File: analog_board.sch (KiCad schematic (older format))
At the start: 54 parts, among them J301 SAMTEC-TSW-105-07-X-D, J302 SAMTEC-TSW-105-07-X-D, J304 SAMTEC-TSW-105-07-X-D, J305 SAMTEC-TSW-105-07-X-D, U1 LM324, U3 AD620, U4 AD620

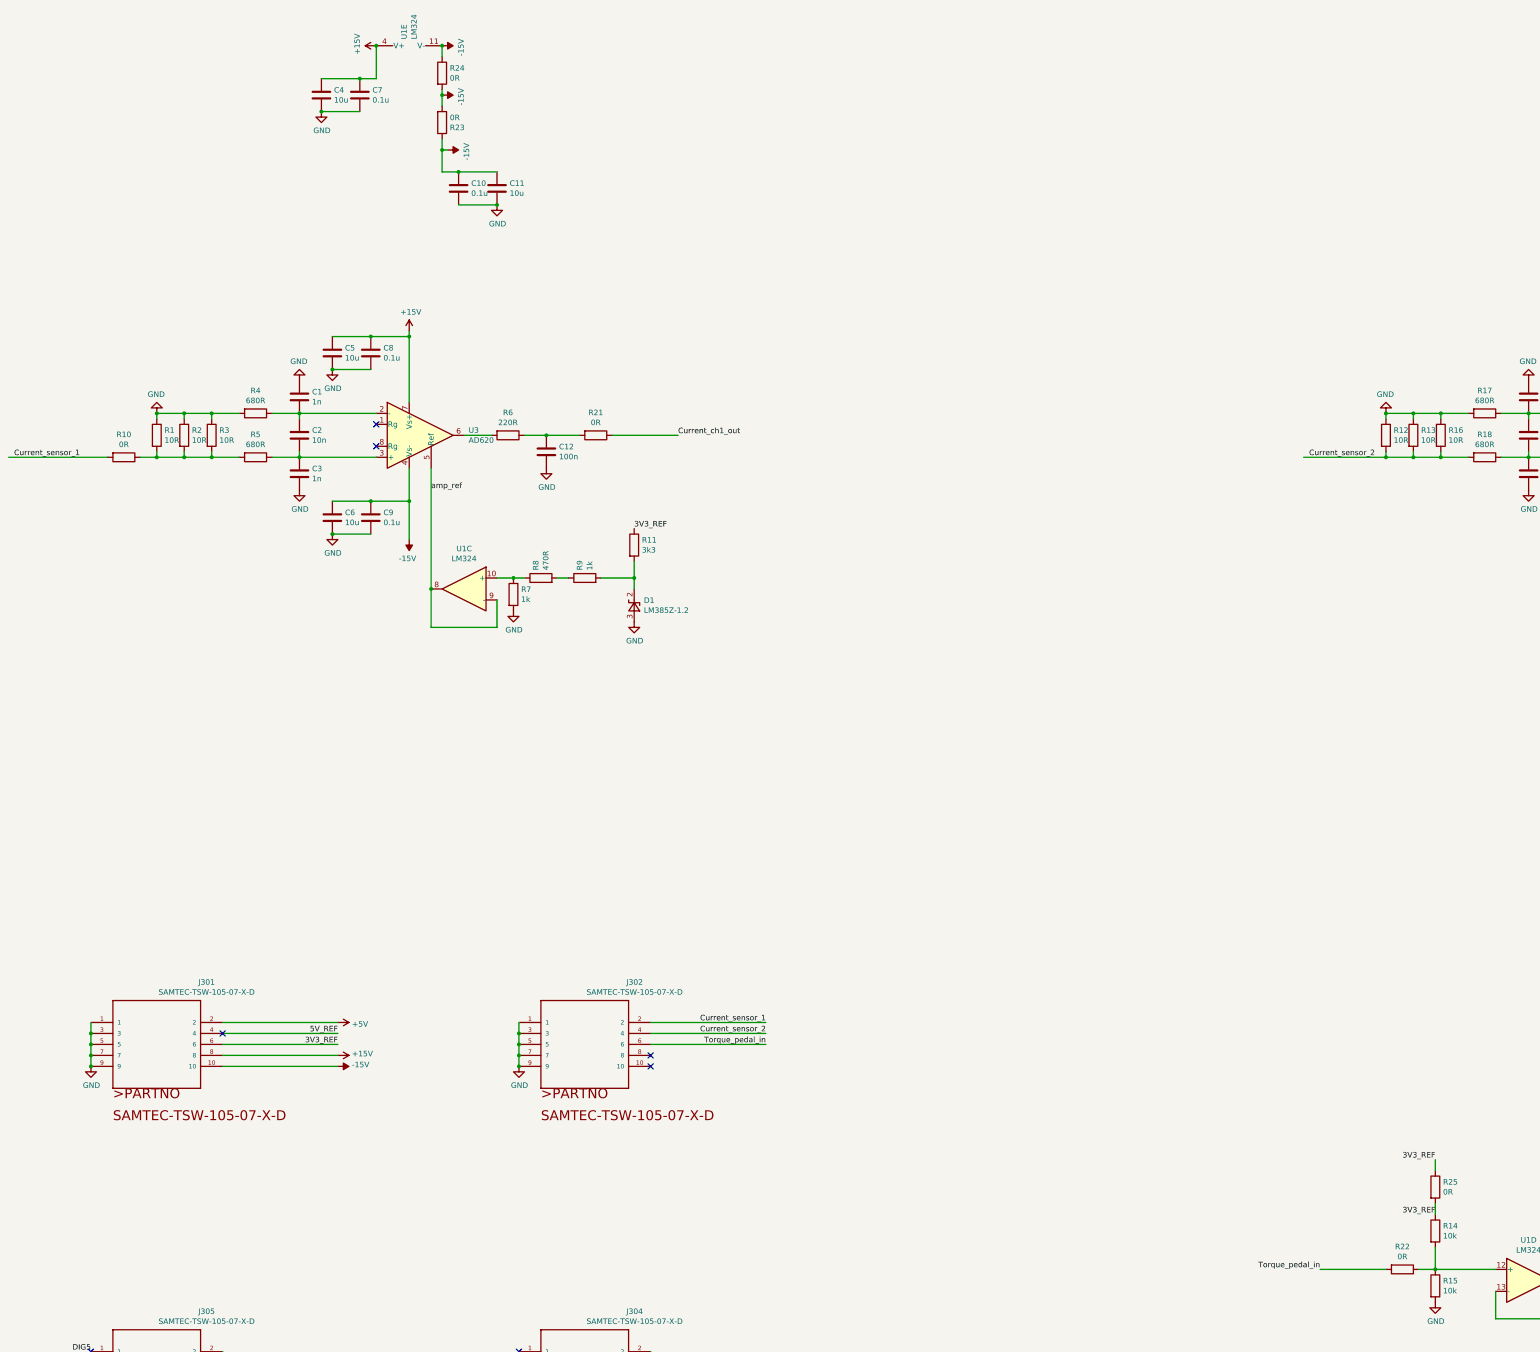
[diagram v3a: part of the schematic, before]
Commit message: Removed OR jumers. Realigned connectors. Moved large components to Bottom. Thickened tracks.
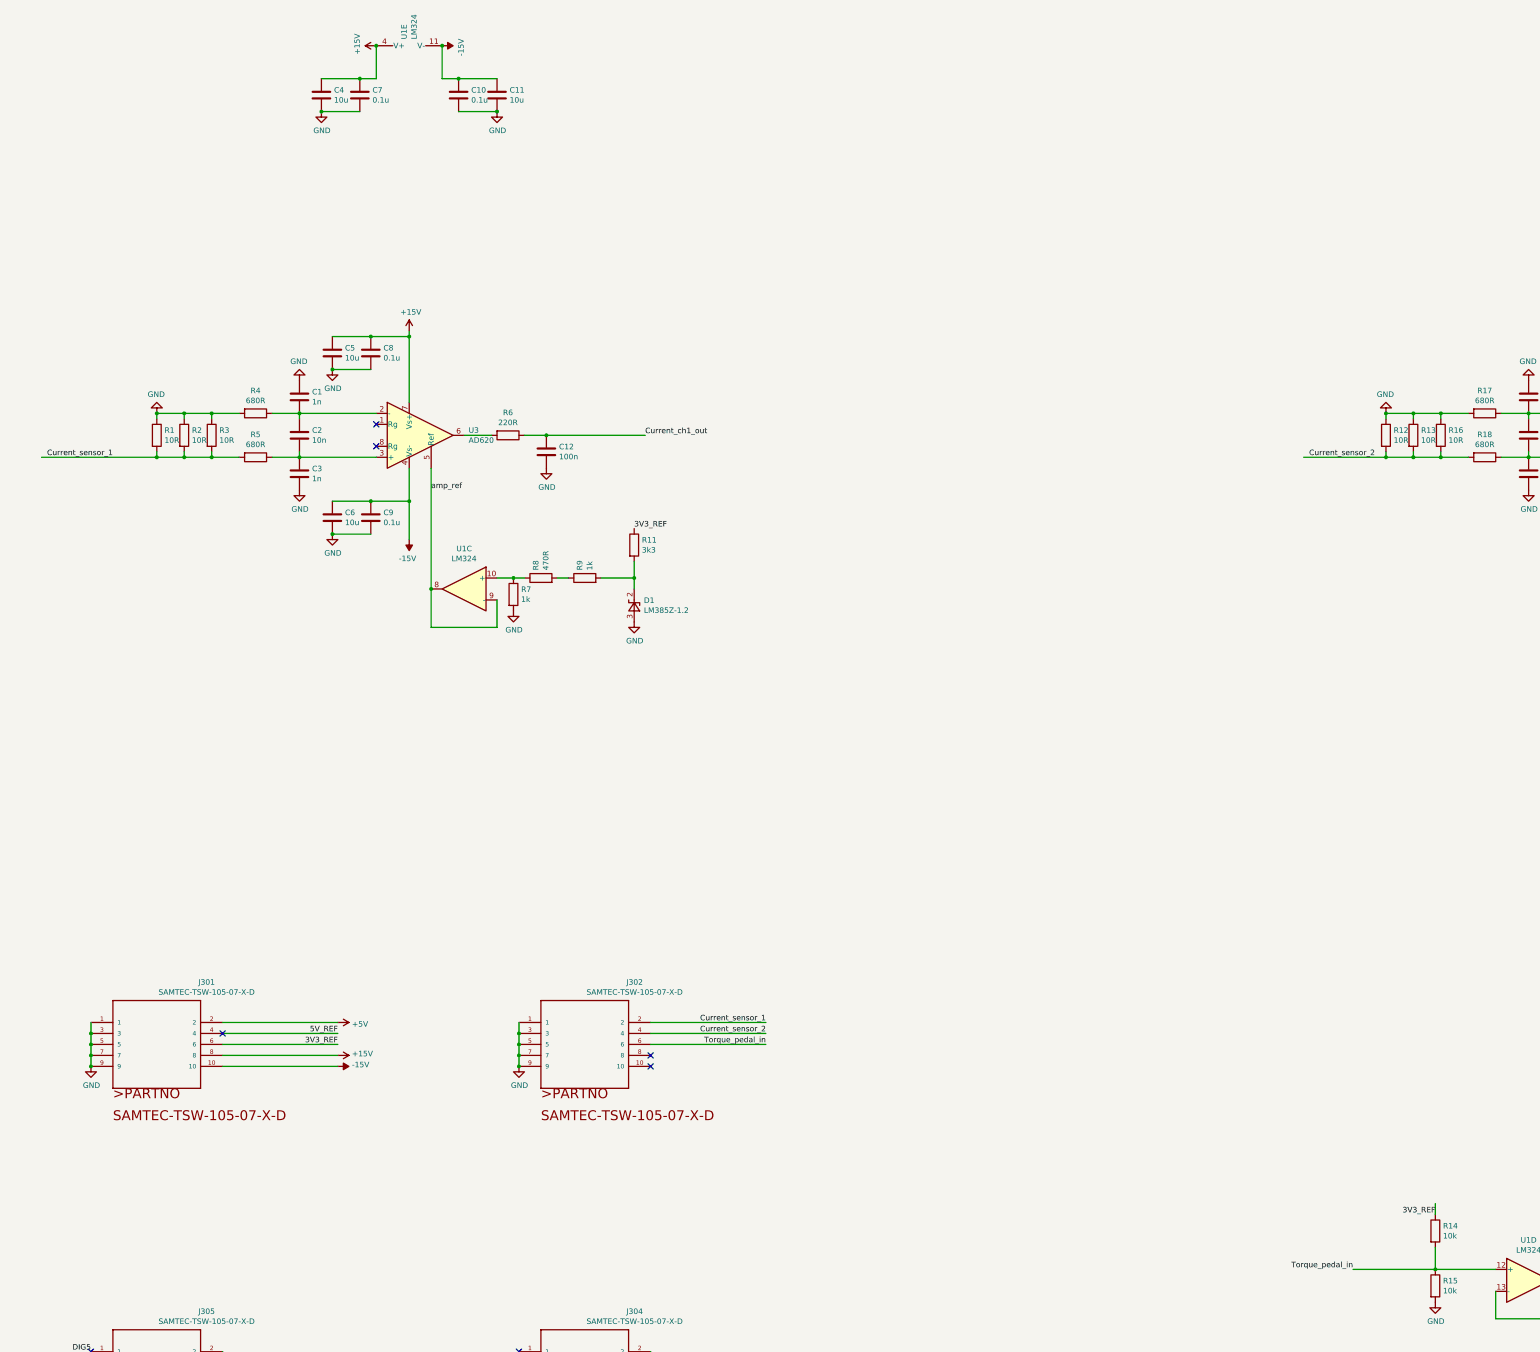
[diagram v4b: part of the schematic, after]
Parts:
- removed R10, R21, R22, R24, R25: 0R, Resistor_SMD:R_1206_3216Metric_Pad1.42x1.75mm_HandSolder, symbol Device:R
- removed R23: 0R, Resistor_SMD:R_0805_2012Metric_Pad1.15x1.40mm_HandSolder, symbol Device:R
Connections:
- net Current_ch1_out: now also C12.1, R6.1
- net Current_sensor_1: now also R1.2, R2.2, R3.2, R5.2
- net Torque_pedal_in: now also R14.2, R15.1, U1.12 (+)
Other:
- moved on the sheet: C10, C11
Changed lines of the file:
@@
 	1    0    0    -1
 $EndComp
-Text Label 850  4800 0    50   ~ 0
+Text Label 1150 4800 0    50   ~ 0
 Current_sensor_1
 $Comp
@@
 Wire Wire Line
 	5250 6100 5250 6350
-Wire Wire Line
-	6900 4600 6300 4600
-Text Label 6900 4600 0    50   ~ 0
+Text Label 6600 4600 0    50   ~ 0
 Current_ch1_out
 Wire Wire Line
@@
 L Device:C C11
 U 1 1 5C74975A
-P 5250 2350
-F 0 "C11" H 5365 2396 50  0000 L CNN
-F 1 "10u" H 5365 2305 50  0000 L CNN
-F 2 "Capacitor_SMD:C_0805_2012Metric_Pad1.15x1.40mm_HandSolder" H 5288 2200 50  0001 C CNN
-F 3 "~" H 5250 2350 50  0001 C CNN
-	1    5250 2350
+P 5250 1500
+F 0 "C11" H 5365 1546 50  0000 L CNN
+F 1 "10u" H 5365 1455 50  0000 L CNN
+F 2 "Capacitor_SMD:C_0805_2012Metric_Pad1.15x1.40mm_HandSolder" H 5288 1350 50  0001 C CNN
+F 3 "~" H 5250 1500 50  0001 C CNN
+	1    5250 1500
 	1    0    0    -1
 $EndComp
@@
 L power:GND #PWR0116
 U 1 1 5C749765
-P 5250 2500
-F 0 "#PWR0116" H 5250 2250 50  0001 C CNN
-F 1 "GND" H 5255 2327 50  0000 C CNN
-F 2 "" H 5250 2500 50  0001 C CNN
-F 3 "" H 5250 2500 50  0001 C CNN
-	1    5250 2500
+P 5250 1650
+F 0 "#PWR0116" H 5250 1400 50  0001 C CNN
+F 1 "GND" H 5255 1477 50  0000 C CNN
+F 2 "" H 5250 1650 50  0001 C CNN
+F 3 "" H 5250 1650 50  0001 C CNN
+	1    5250 1650
 	1    0    0    -1
 $EndComp
@@
 L Device:C C10
 U 1 1 5C7542C0
-P 4900 2350
-F 0 "C10" H 5015 2396 50  0000 L CNN
-F 1 "0.1u" H 5015 2305 50  0000 L CNN
-F 2 "Capacitor_SMD:C_0805_2012Metric_Pad1.15x1.40mm_HandSolder" H 4938 2200 50  0001 C CNN
-F 3 "~" H 4900 2350 50  0001 C CNN
-	1    4900 2350
-	1    0    0    -1
-$EndComp
-Wire Wire Line
-	4900 2200 5250 2200
-Wire Wire Line
-	4900 2500 5250 2500
-Connection ~ 5250 2500
+P 4900 1500
+F 0 "C10" H 5015 1546 50  0000 L CNN
+F 1 "0.1u" H 5015 1455 50  0000 L CNN
+F 2 "Capacitor_SMD:C_0805_2012Metric_Pad1.15x1.40mm_HandSolder" H 4938 1350 50  0001 C CNN
+F 3 "~" H 4900 1500 50  0001 C CNN
+	1    4900 1500
+	1    0    0    -1
+$EndComp
+Wire Wire Line
+	4900 1350 5250 1350
+Wire Wire Line
+	4900 1650 5250 1650
+Connection ~ 5250 1650
 Wire Wire Line
 	4000 1350 4150 1350
@@
 Connection ~ 4150 1050
 Wire Wire Line
-	4900 2200 4750 2200
-Wire Wire Line
-	4750 2200 4750 2000
-Connection ~ 4900 2200
+	4900 1350 4750 1350
+Connection ~ 4900 1350
 $Comp
 L power:+5V #PWR0117
@@
 	1    0    0    -1
 $EndComp
-Text Label 13800 11200 2    50   ~ 0
-3V3_REF
-Text Label 12750 12200 2    50   ~ 0
+Text Label 13050 12200 2    50   ~ 0
 Torque_pedal_in
 Wire Wire Line
@@
 Wire Wire Line
 	15850 4900 15850 5100
-$Comp
-L Device:R R10
-U 1 1 5C792D0B
-P 1850 4800
-F 0 "R10" V 1643 4800 50  0000 C CNN
-F 1 "0R" V 1734 4800 50  0000 C CNN
-F 2 "Resistor_SMD:R_1206_3216Metric_Pad1.42x1.75mm_HandSolder" V 1780 4800 50  0001 C CNN
-F 3 "~" H 1850 4800 50  0001 C CNN
-	1    1850 4800
-	0    1    1    0
-$EndComp
-Wire Wire Line
-	800  4800 1700 4800
-Wire Wire Line
-	2000 4800 2150 4800
 Connection ~ 2150 4800
-$Comp
-L Device:R R21
-U 1 1 5C7A1976
-P 6150 4600
-F 0 "R21" V 5943 4600 50  0000 C CNN
-F 1 "0R" V 6034 4600 50  0000 C CNN
-F 2 "Resistor_SMD:R_1206_3216Metric_Pad1.42x1.75mm_HandSolder" V 6080 4600 50  0001 C CNN
-F 3 "~" H 6150 4600 50  0001 C CNN
-	1    6150 4600
-	0    1    1    0
-$EndComp
-Wire Wire Line
-	5700 4600 6000 4600
 Connection ~ 5700 4600
-$Comp
-L Device:R R22
-U 1 1 5C7B8DFC
-P 13500 12200
-F 0 "R22" V 13293 12200 50  0000 C CNN
-F 1 "0R" V 13384 12200 50  0000 C CNN
-F 2 "Resistor_SMD:R_1206_3216Metric_Pad1.42x1.75mm_HandSolder" V 13430 12200 50  0001 C CNN
-F 3 "~" H 13500 12200 50  0001 C CNN
-	1    13500 12200
-	0    1    1    0
-$EndComp
-Wire Wire Line
-	13800 12200 13650 12200
-Wire Wire Line
-	13350 12200 12750 12200
-$Comp
-L Device:R R23
-U 1 1 5C7D3DFD
-P 4750 1750
-F 0 "R23" H 4820 1796 50  0000 L CNN
-F 1 "0R" H 4820 1705 50  0000 L CNN
-F 2 "Resistor_SMD:R_0805_2012Metric_Pad1.15x1.40mm_HandSolder" V 4680 1750 50  0001 C CNN
-F 3 "~" H 4750 1750 50  0001 C CNN
-	1    4750 1750
-	1    0    0    1
-$EndComp
-$Comp
-L power:-15V #PWR0128
-U 1 1 5C7F0418
-P 4800 2000
-F 0 "#PWR0128" H 4800 2100 50  0001 C CNN
-F 1 "-15V" H 4815 2173 50  0000 C CNN
-F 2 "" H 4800 2000 50  0001 C CNN
-F 3 "" H 4800 2000 50  0001 C CNN
-	1    4800 2000
-	0    1    1    0
-$EndComp
-Wire Wire Line
-	4800 2000 4750 2000
-Connection ~ 4750 2000
-Wire Wire Line
-	4750 2000 4750 1900
-$Comp
-L Device:R R24
-U 1 1 5C80067D
-P 4750 1300
-F 0 "R24" H 4820 1346 50  0000 L CNN
-F 1 "0R" H 4820 1255 50  0000 L CNN
-F 2 "Resistor_SMD:R_1206_3216Metric_Pad1.42x1.75mm_HandSolder" V 4680 1300 50  0001 C CNN
-F 3 "~" H 4750 1300 50  0001 C CNN
-	1    4750 1300
-	1    0    0    -1
-$EndComp
-Wire Wire Line
-	4750 1150 4750 1050
 Connection ~ 4750 1050
 Wire Wire Line
-	4750 1450 4750 1500
-$Comp
-L Device:R R25
-U 1 1 5C7CD4AE
-P 13800 11450
-F 0 "R25" H 13870 11496 50  0000 L CNN
-F 1 "0R" H 13870 11405 50  0000 L CNN
-F 2 "Resistor_SMD:R_1206_3216Metric_Pad1.42x1.75mm_HandSolder" V 13730 11450 50  0001 C CNN
-F 3 "~" H 13800 11450 50  0001 C CNN
-	1    13800 11450
-	1    0    0    -1
-$EndComp
-Wire Wire Line
 	13800 11700 13800 11600
-Wire Wire Line
-	13800 11300 13800 11200
 Wire Wire Line
 	1550 10150 1550 10250
@@
 Text Label 13800 11700 2    50   ~ 0
 3V3_REF
-$Comp
-L power:-15V #PWR?
-U 1 1 5C7C6022
-P 4750 1500
-F 0 "#PWR?" H 4750 1600 50  0001 C CNN
-F 1 "-15V" H 4765 1673 50  0000 C CNN
-F 2 "" H 4750 1500 50  0001 C CNN
-F 3 "" H 4750 1500 50  0001 C CNN
-	1    4750 1500
-	0    1    1    0
-$EndComp
-Connection ~ 4750 1500
-Wire Wire Line
-	4750 1500 4750 1600
+Wire Wire Line
+	4750 1050 4750 1350
+Wire Wire Line
+	1100 4800 2150 4800
+Wire Wire Line
+	5700 4600 6600 4600
+Wire Wire Line
+	13050 12200 13800 12200
 $EndSCHEMATC

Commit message: Added test points and ground fill on top
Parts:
- added C13, C17: 1n, Capacitor_SMD:C_0805_2012Metric_Pad1.15x1.40mm_HandSolder, symbol Device:C
- added TP1: TP_Isense1, TestPoint:TestPoint_2Pads_Pitch2.54mm_Drill0.8mm, symbol Connector:TestPoint_2Pole
- added TP10: TP_pedalB, TestPoint:TestPoint_2Pads_Pitch2.54mm_Drill0.8mm, symbol Connector:TestPoint_2Pole
- added TP11: TP_ch2_outA, TestPoint:TestPoint_2Pads_Pitch2.54mm_Drill0.8mm, symbol Connector:TestPoint_2Pole
- added TP12: TP_ch2_ref, TestPoint:TestPoint_2Pads_Pitch2.54mm_Drill0.8mm, symbol Connector:TestPoint_2Pole
- added TP13: TP_ch2_outB, TestPoint:TestPoint_2Pads_Pitch2.54mm_Drill0.8mm, symbol Connector:TestPoint_2Pole
- added TP2: TP_A1in, TestPoint:TestPoint_2Pads_Pitch2.54mm_Drill0.8mm, symbol Connector:TestPoint_2Pole
- added TP3: TP_ch1_outA, TestPoint:TestPoint_2Pads_Pitch2.54mm_Drill0.8mm, symbol Connector:TestPoint_2Pole
- added TP4: TP_ch1_ref, TestPoint:TestPoint_2Pads_Pitch2.54mm_Drill0.8mm, symbol Connector:TestPoint_2Pole
- added TP5: TP_ch1_outB, TestPoint:TestPoint_2Pads_Pitch2.54mm_Drill0.8mm, symbol Connector:TestPoint_2Pole
- added TP6: TP_Isense2, TestPoint:TestPoint_2Pads_Pitch2.54mm_Drill0.8mm, symbol Connector:TestPoint_2Pole
- added TP7: TP_pedal_in, TestPoint:TestPoint_2Pads_Pitch2.54mm_Drill0.8mm, symbol Connector:TestPoint_2Pole
- added TP8: TP_A2in, TestPoint:TestPoint_2Pads_Pitch2.54mm_Drill0.8mm, symbol Connector:TestPoint_2Pole
- added TP9: TP_pedalA, TestPoint:TestPoint_2Pads_Pitch2.54mm_Drill0.8mm, symbol Connector:TestPoint_2Pole
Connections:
- net Current_ch1_out: now also TP5.1
- net Current_ch2_out: now also TP13.1
- net Current_sensor_1: now also TP1.1
- net Current_sensor_2: now also TP6.1
- net GND: now also C13.1, C17.1, TP1.2, TP10.2, TP11.2, TP12.2, TP13.2, TP3.2, TP4.2, TP5.2, TP6.2, TP7.2, TP9.2
- net Torque_pedal_ADC: now also TP10.1
- net Torque_pedal_in: now also TP7.1
- net amp_ref: now also C13.2, C17.2, TP12.1, TP4.1
- net at C1.2, C2.1, R4.1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: now also TP2.1
- net at C2.2, C3.1, R5.1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: now also TP2.2
- net at R6.2, U3.6: now also TP3.1
- net at C14.2, C15.1, R17.1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: now also TP8.1
- net at C15.2, C16.1, R18.1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: now also TP8.2
- net at R20.2, U4.6: now also TP11.1
- net at R19.2, U1.13 (-), U1.14: now also TP9.1
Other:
- moved on the sheet: C23, D1, R11, R14, R15, R19, R7, R8, R9, U1C, U1D
